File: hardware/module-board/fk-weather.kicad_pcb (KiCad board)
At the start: 2 copper layers, 37.5 x 103 mm, 71 parts, among them J1 MICRO-USB, J10 Conn_01x06, J11 Conn_01x06, J2 Conn_01x05, J3 CONN_01x03_SERIAL, J4 Conn_01x04, J5 Conn_01x02, J6 CONN_02x05_SWD, Q4 2N7002LT1G, SW1 SPNO, U1 ATSAMD21G18A-AU, U2 MCP1700T-XXX2E, U3 TPS2041B, U4 S25FL1xxK0XM, U5 SK6812, U6 PCF8523, Y1 FC-135, Y2 FC-135

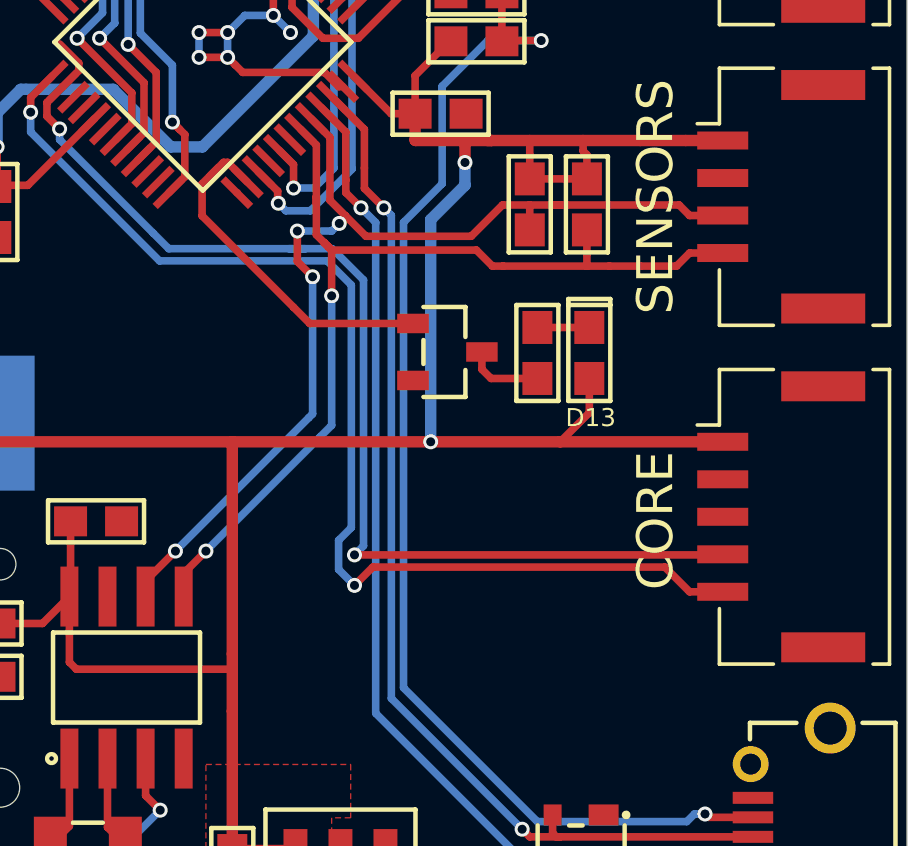
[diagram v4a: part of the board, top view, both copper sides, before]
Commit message: Add a second core port.
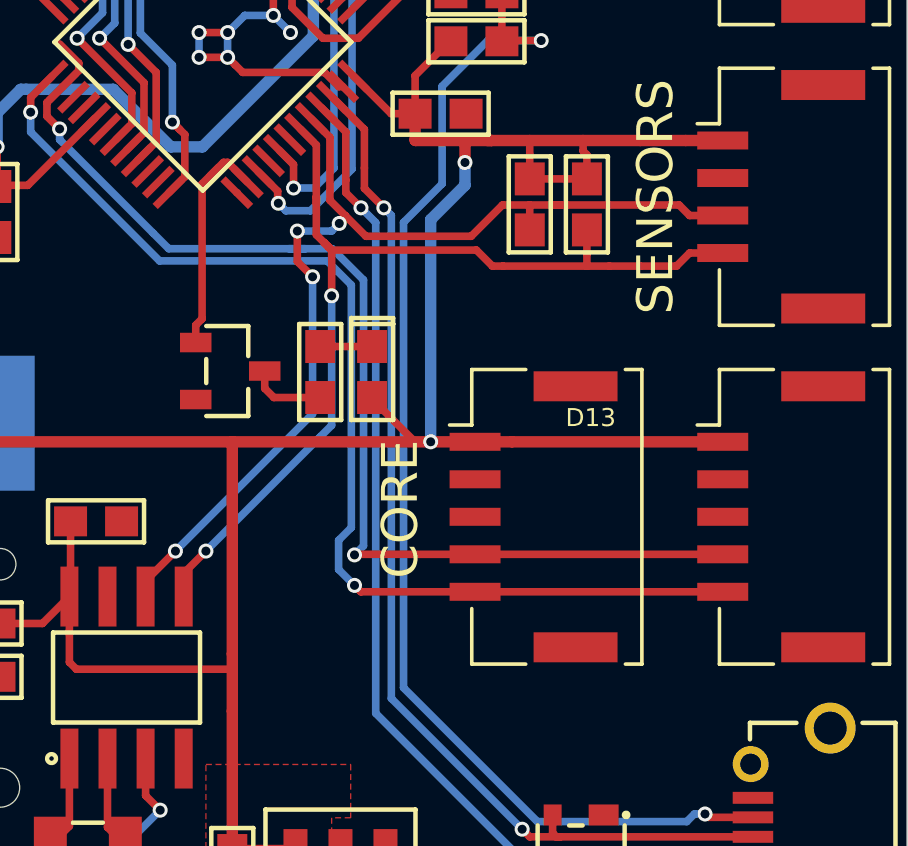
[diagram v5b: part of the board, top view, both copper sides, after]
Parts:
- added J7: Conn_01x05, conservify:Molex_CLIK-Mate_502382-0570_1x05_P1.25mm_Vertical, F.Cu at (109.6, 179.1)
- moved D5 7.27 mm to (104.2, 174.2)
- moved Q4 7.27 mm to (99.5, 174.2)
- moved R17 7.27 mm to (102.5, 174.2)
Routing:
- net /D13: track 12.0 -> 7.82 mm
- net /SDA2: track 38.2 -> 37.7 mm

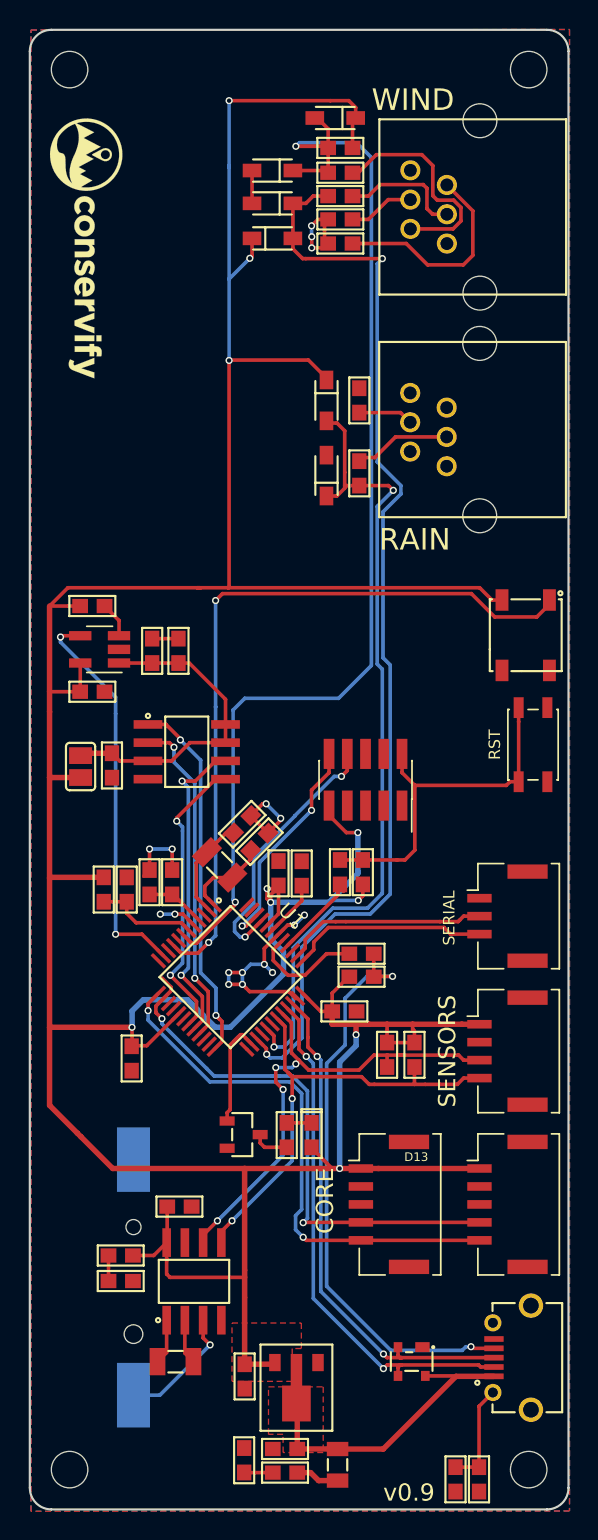
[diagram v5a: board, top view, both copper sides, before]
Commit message: Nudge holes to match Core pattern, which needed a little more room.
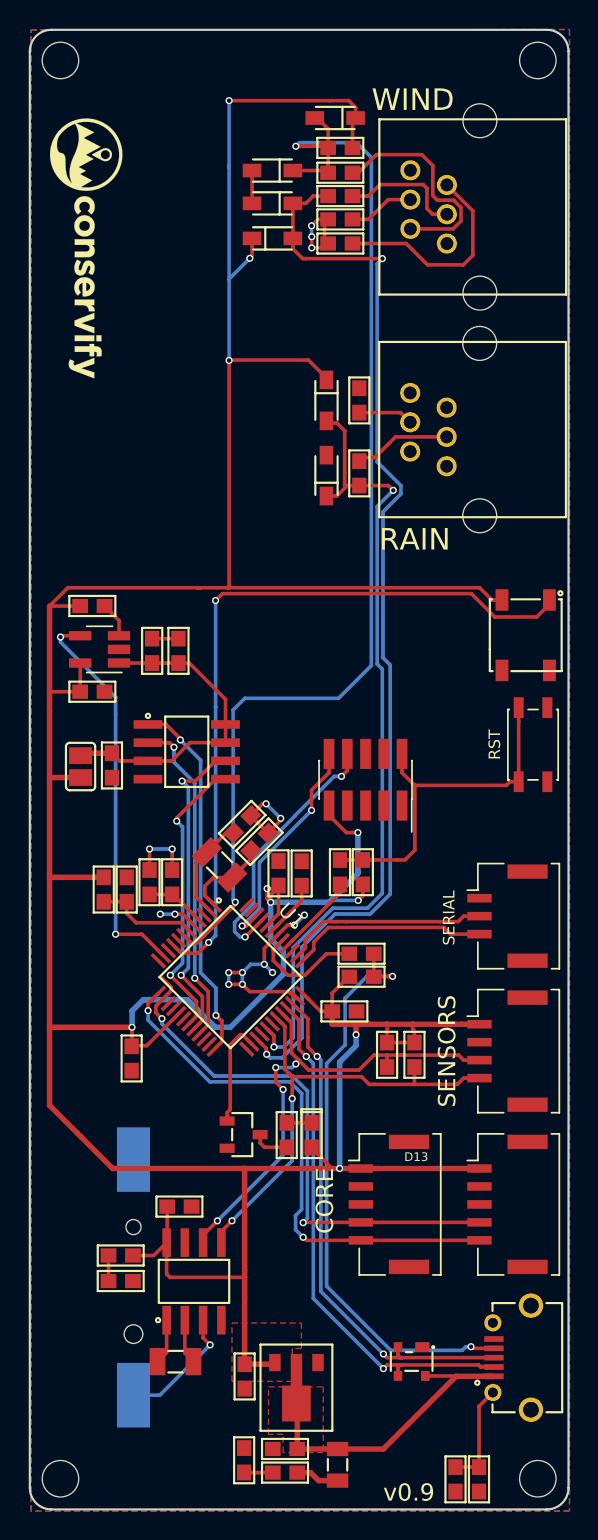
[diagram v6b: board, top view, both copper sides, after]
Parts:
- removed the REF** at (87.4, 100.1)
- removed the REF** at (87.4, 197.5)
- removed the REF** at (119.3, 197.5)
- removed the REF** at (119.3, 100.1)
- added REF**: HOLE_NPTH_2.54MM, conservify:HOLE_NPTH_2.54MM, F.Cu at (86.7, 99.4)
- added REF**: HOLE_NPTH_2.54MM, conservify:HOLE_NPTH_2.54MM, F.Cu at (86.7, 198.2)
- added REF**: HOLE_NPTH_2.54MM, conservify:HOLE_NPTH_2.54MM, F.Cu at (120.0, 198.2)
- added REF**: HOLE_NPTH_2.54MM, conservify:HOLE_NPTH_2.54MM, F.Cu at (120.0, 99.4)
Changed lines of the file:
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@@
     (links 157)
     (no_connects 0)
-    (area 84.528444 97.227082 122.178446 200.377084)
+    (area 83.195572 92.413321 123.685 216.839714)
     (thickness 1.6)
     (drawings 16)
@@
   )
   (setup
-    (last_trace_width 0.381)
+    (last_trace_width 0.254)
     (user_trace_width 0.2032)
     (user_trace_width 0.254)
@@
   )
   (module conservify:HOLE_NPTH_2.54MM (layer F.Cu)
-    (at 87.373445 100.072083 90)
+    (at 86.738445 99.437083 90)
     (fp_text reference REF** (at 0 -2.54 90) (layer F.SilkS) hide
       (effects (font (size 1 1) (thickness 0.15)))
@@
   )
   (module conservify:HOLE_NPTH_2.54MM (layer F.Cu)
-    (at 87.373445 197.532083 90)
+    (at 86.738445 198.167083 90)
     (fp_text reference REF** (at 0 -2.54 90) (layer F.SilkS) hide
       (effects (font (size 1 1) (thickness 0.15)))
@@
   )
   (module conservify:HOLE_NPTH_2.54MM (layer F.Cu)
-    (at 119.333445 197.532083 90)
+    (at 119.968445 198.167083 90)
     (fp_text reference REF** (at 0 -2.54 90) (layer F.SilkS) hide
       (effects (font (size 1 1) (thickness 0.15)))
@@
   )
   (module conservify:HOLE_NPTH_2.54MM (layer F.Cu)
-    (at 119.333445 100.072083 90)
+    (at 119.968445 99.437083 90)
     (fp_text reference REF** (at 0 -2.54 90) (layer F.SilkS) hide
       (effects (font (size 1 1) (thickness 0.15)))

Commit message: Part for load switch was wrong, fixing.
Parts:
- U3: value TPS2041B -> TPS2051B
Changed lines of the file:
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@@
     (links 157)
     (no_connects 0)
-    (area 83.195572 92.413321 123.685 216.839714)
+    (area 84.528444 97.227082 122.178446 200.377084)
     (thickness 1.6)
     (drawings 16)
@@
       (effects (font (size 1 1) (thickness 0.15)))
     )
-    (fp_text value TPS2041B (at 0 2.9 180) (layer F.Fab)
-      (effects (font (size 1 1) (thickness 0.15)))
-    )
+    (fp_text value TPS2051B (at 0 2.9 180) (layer F.Fab)
+      (effects (font (size 1 1) (thickness 0.15)))
+    )
